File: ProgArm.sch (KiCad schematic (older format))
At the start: 130 parts, among them K1 RING_LEDS_Port, M1 MOTOR, P1 I²C_Port, P10 RING_VCC, P11 RING_GND, P12 RING_GPIOA_4_Port, P13 RING_GPIOA_3_Port, P14 RXD, P15 RING_BUTTONS_Port, P16 MicroUSB, P2 SPI_Port, P3 UART_Port, P4 SWD_Port, P5 GPIOA_1_2_Port, P6 TIM1_Port, P7 T_SENS, P8 RING_IR_OUT, P9 TXD, Q1 MOS_P, Q2 MOS_P, Q3 MOS_P, Q4 MOS_P, Q5 MOS_P, Q6 MOS_P, Q7 MOS_P, Q8 MOS_P, SW1 FW/RST, SW2 ON/OFF, U1 TPS78330, U2 BQ24297, U3 LM3668, U4 STM32F103R, U5 MPU9250, U6 BQ27410, U7 SI1143, U8 LPS25H, U9 NRF8001, X1 32.768kHz, X2 8MHz, X3 16MHz

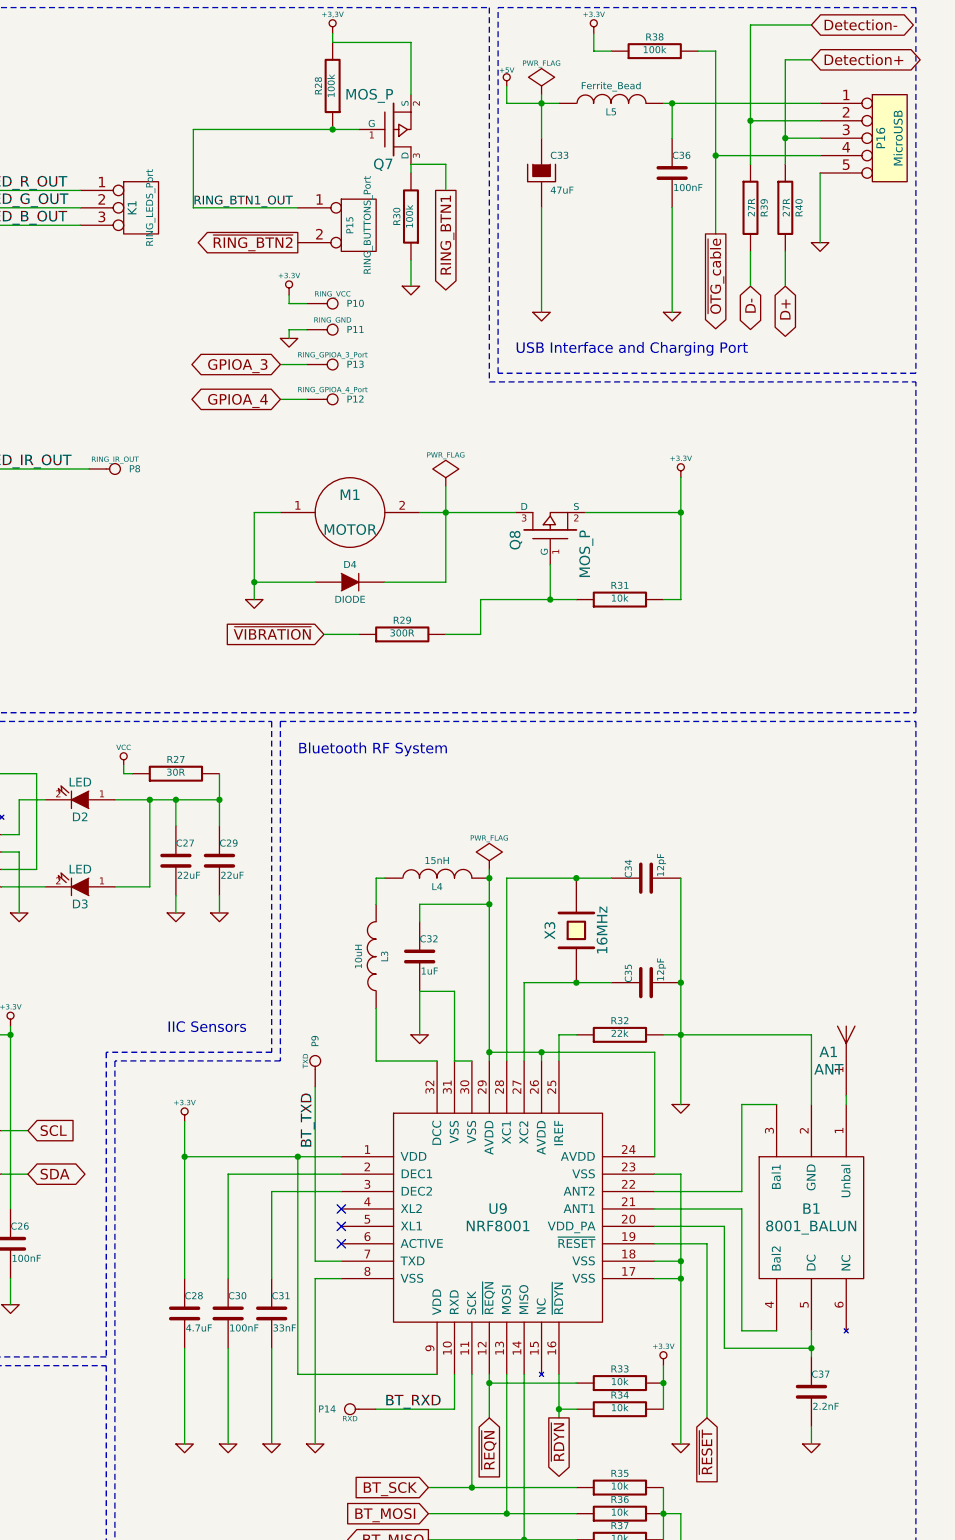
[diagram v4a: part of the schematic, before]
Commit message: Started assigning footprints
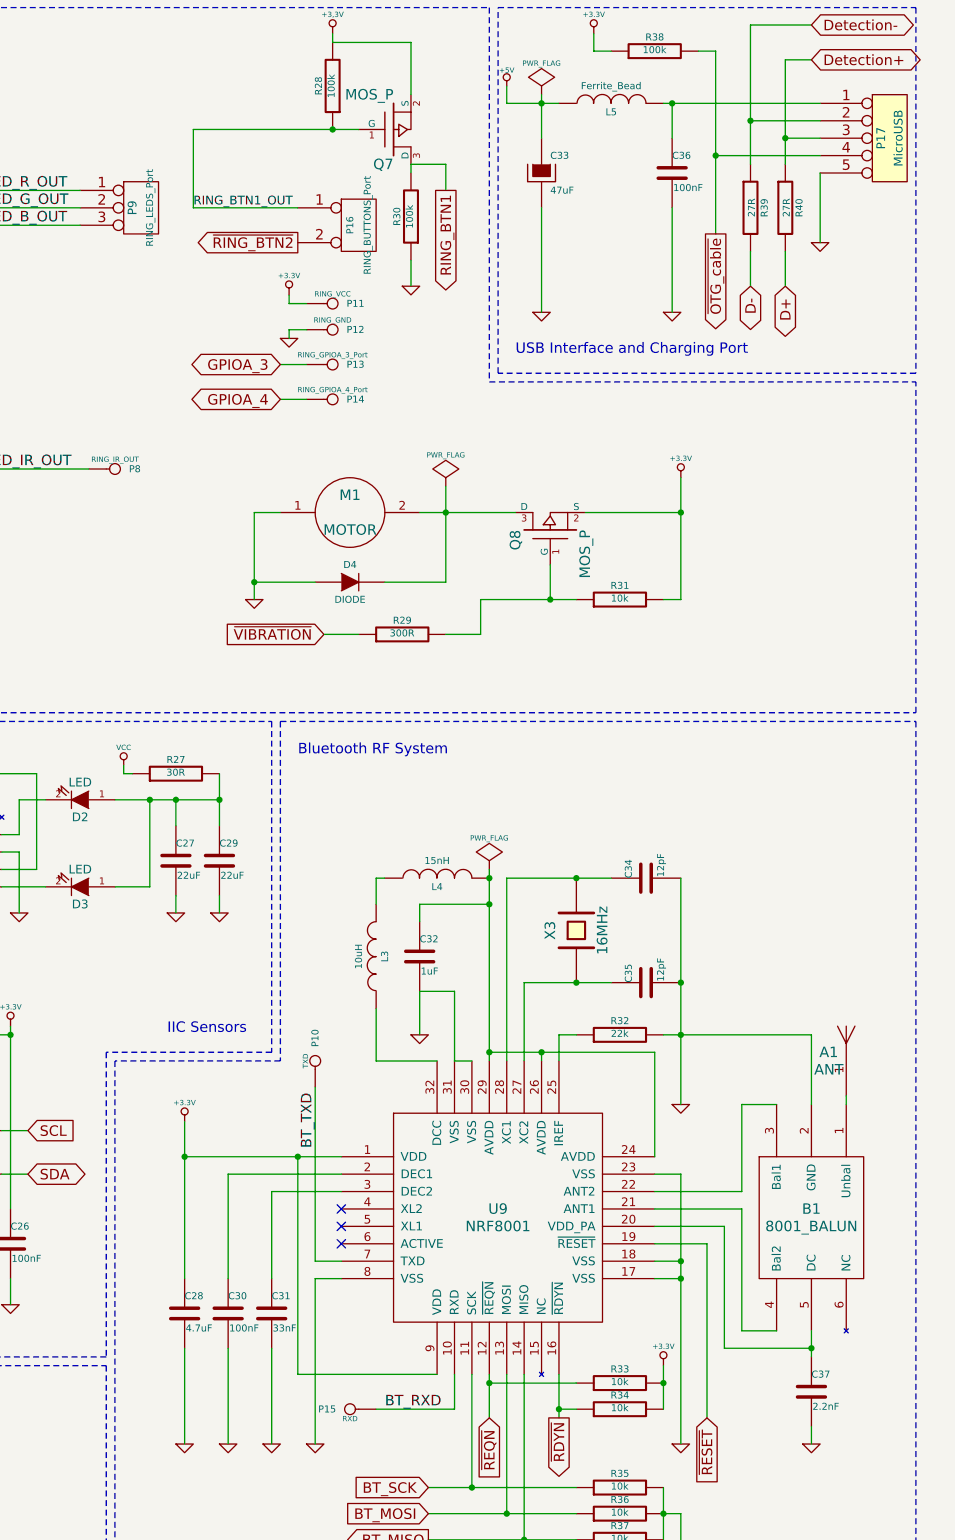
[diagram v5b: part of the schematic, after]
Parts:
- renumbered P9 to P10, P10 to P11, P11 to P12, P12 to P14, P14 to P15, P15 to P16, P16 to P17, K1 to P9
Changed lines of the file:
@@
 $EndComp
 $Comp
-L CONN_5 P16
+L CONN_5 P17
 U 1 1 52F41441
 P 15850 1300
-F 0 "P16" V 15800 1300 50  0000 C CNN
+F 0 "P17" V 15800 1300 50  0000 C CNN
 F 1 "MicroUSB" V 15900 1300 50  0000 C CNN
 F 2 "" H 15850 1300 60  0000 C CNN
@@
 	12550 7750 12700 7750
 $Comp
-L CONN_1 P14
+L CONN_1 P15
 U 1 1 547E9AC3
 P 12750 8600
-F 0 "P14" H 12830 8600 40  0000 L CNN
+F 0 "P15" H 12830 8600 40  0000 L CNN
 F 1 "RXD" H 12750 8655 30  0000 C CNN
 F 2 "" H 12750 8600 60  0000 C CNN
@@
 $EndComp
 $Comp
-L CONN_1 P9
+L CONN_1 P10
 U 1 1 547E9AF8
 P 12550 6600
-F 0 "P9" H 12630 6600 40  0000 L CNN
+F 0 "P10" H 12630 6600 40  0000 L CNN
 F 1 "TXD" H 12550 6655 30  0000 C CNN
 F 2 "" H 12550 6600 60  0000 C CNN
@@
 BT_RXD
 $Comp
-L CONN_3 K1
+L CONN_3 P9
 U 1 1 54824D0C
 P 11550 1700
-F 0 "K1" V 11500 1700 50  0000 C CNN
+F 0 "P9" V 11500 1700 50  0000 C CNN
 F 1 "RING_LEDS_Port" V 11600 1700 40  0000 C CNN
 F 2 "" H 11550 1700 60  0000 C CNN
@@
 LED_IR_OUT
 $Comp
-L CONN_2 P15
+L CONN_2 P16
 U 1 1 5482656C
 P 12800 1800
-F 0 "P15" V 12750 1800 40  0000 C CNN
+F 0 "P16" V 12750 1800 40  0000 C CNN
 F 1 "RING_BUTTONS_Port" V 12850 1800 40  0000 C CNN
 F 2 "" H 12800 1800 60  0000 C CNN
@@
 	13100 2150 13100 2000
 $Comp
-L CONN_1 P10
+L CONN_1 P11
 U 1 1 54826928
 P 12650 2250
-F 0 "P10" H 12730 2250 40  0000 L CNN
+F 0 "P11" H 12730 2250 40  0000 L CNN
 F 1 "RING_VCC" H 12650 2305 30  0000 C CNN
 F 2 "" H 12650 2250 60  0000 C CNN
@@
 $EndComp
 $Comp
-L CONN_1 P11
+L CONN_1 P12
 U 1 1 54826937
 P 12650 2400
-F 0 "P11" H 12730 2400 40  0000 L CNN
+F 0 "P12" H 12730 2400 40  0000 L CNN
 F 1 "RING_GND" H 12650 2455 30  0000 C CNN
 F 2 "" H 12650 2400 60  0000 C CNN
@@
 	12500 2400 12400 2400
 $Comp
-L CONN_1 P12
+L CONN_1 P14
 U 1 1 54826154
 P 12650 2800
-F 0 "P12" H 12730 2800 40  0000 L CNN
+F 0 "P14" H 12730 2800 40  0000 L CNN
 F 1 "RING_GPIOA_4_Port" H 12650 2855 30  0000 C CNN
 F 2 "" H 12650 2800 60  0000 C CNN

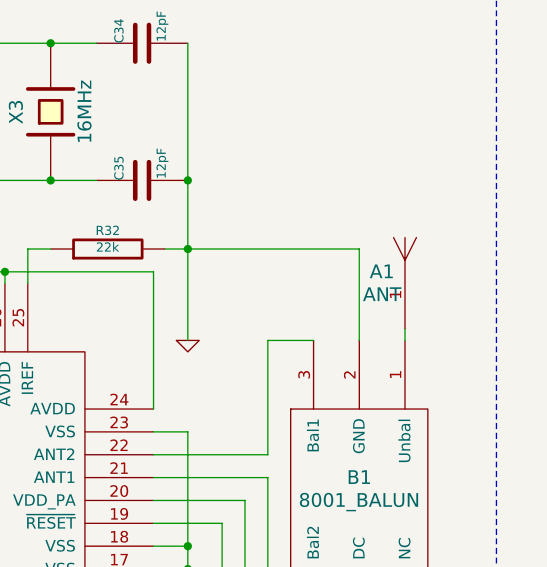
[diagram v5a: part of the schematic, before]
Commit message: Fixed antenna pin number, changed footprints for BT TXD and RXD
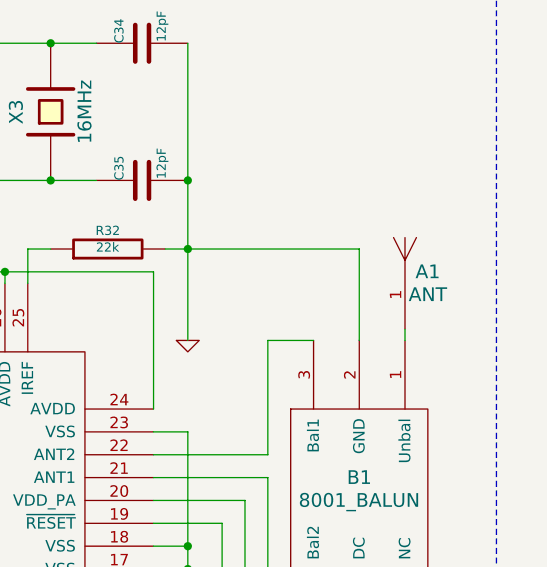
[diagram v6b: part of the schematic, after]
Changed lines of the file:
@@
 Wire Wire Line
 	15400 6450 15400 6850
-$Comp
-L ANT A1
-U 1 1 547E5E7E
-P 15600 6600
-F 0 "A1" H 15500 6650 60  0000 C CNN
-F 1 "ANT" H 15500 6550 60  0000 C CNN
-F 2 "~" H 15500 6650 60  0000 C CNN
-F 3 "~" H 15500 6650 60  0000 C CNN
-	1    15600 6600
-	1    0    0    -1
-$EndComp
 Wire Wire Line
 	15600 6800 15600 6850
@@
 Wire Wire Line
 	4000 2950 4100 2950
+$Comp
+L ANT A1
+U 1 1 5487C6FB
+P 15600 6600
+F 0 "A1" H 15700 6650 60  0000 C CNN
+F 1 "ANT" H 15700 6550 60  0000 C CNN
+F 2 "~" H 15500 6650 60  0000 C CNN
+F 3 "~" H 15500 6650 60  0000 C CNN
+	1    15600 6600
+	1    0    0    -1
+$EndComp
 $EndSCHEMATC
